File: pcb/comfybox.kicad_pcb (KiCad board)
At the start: 2 copper layers, 240 x 130 mm, 21 parts, among them K1 SW_CHOC, K2 SW_CHOC, K3 SW_CHOC, K4 SW_CHOC, P1 SW_CHOC, P2 SW_CHOC, P3 SW_CHOC, P4 SW_CHOC

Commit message: add front ground plane
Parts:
- moved G*** 1.00 mm to (217.5, 135.0)
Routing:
- added copper zone on F.Cu, net GND

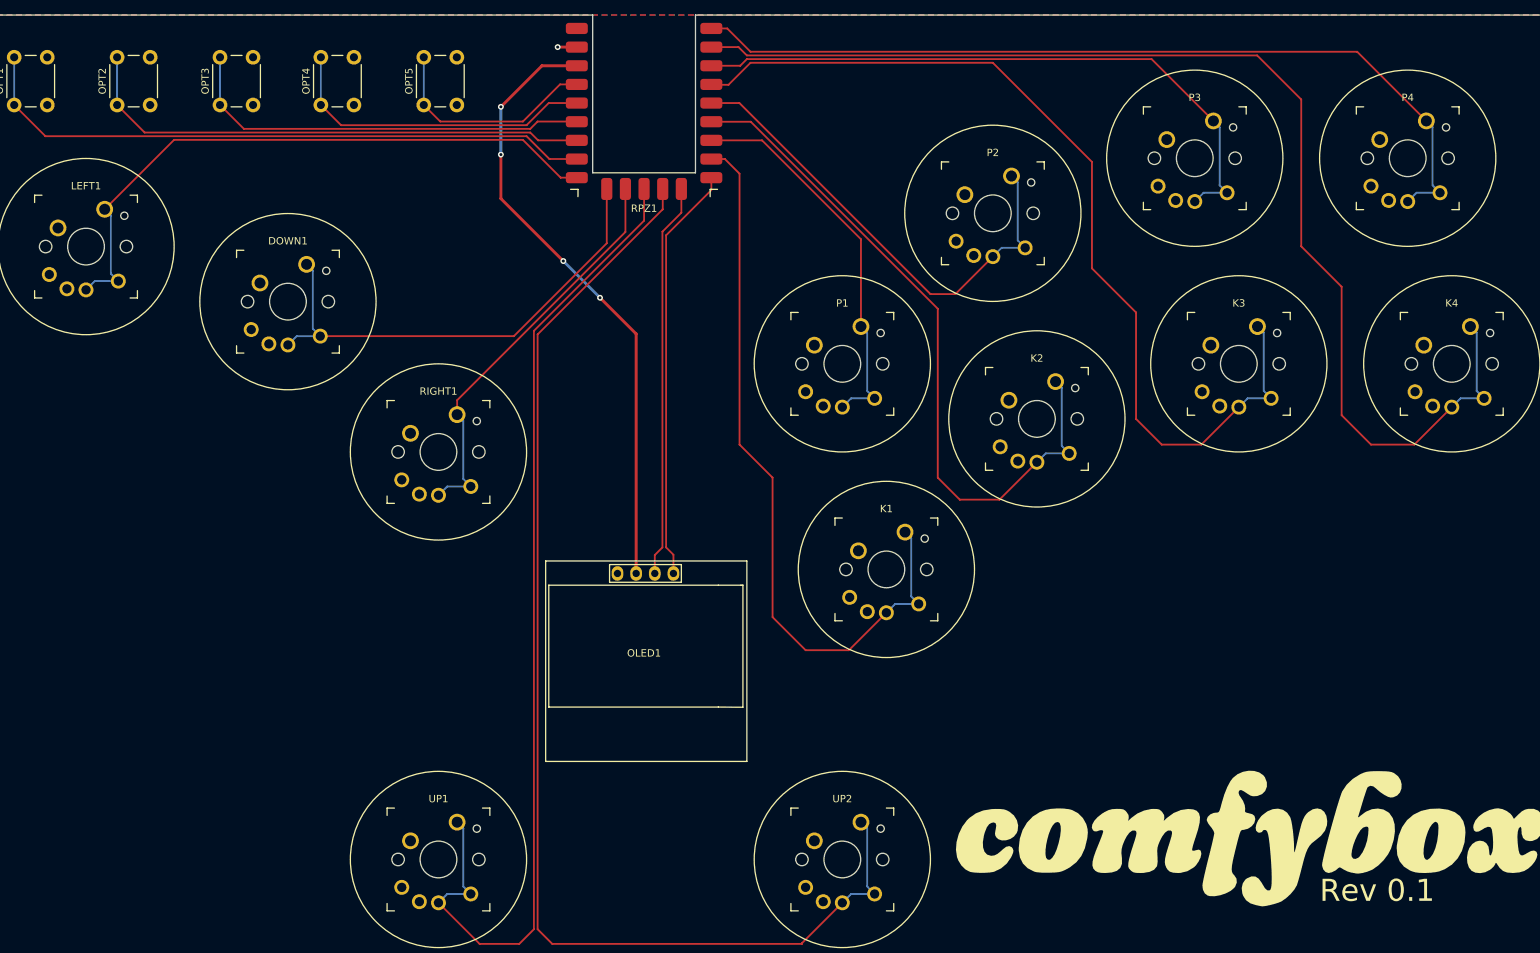
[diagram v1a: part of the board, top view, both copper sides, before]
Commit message: reversible rp2040
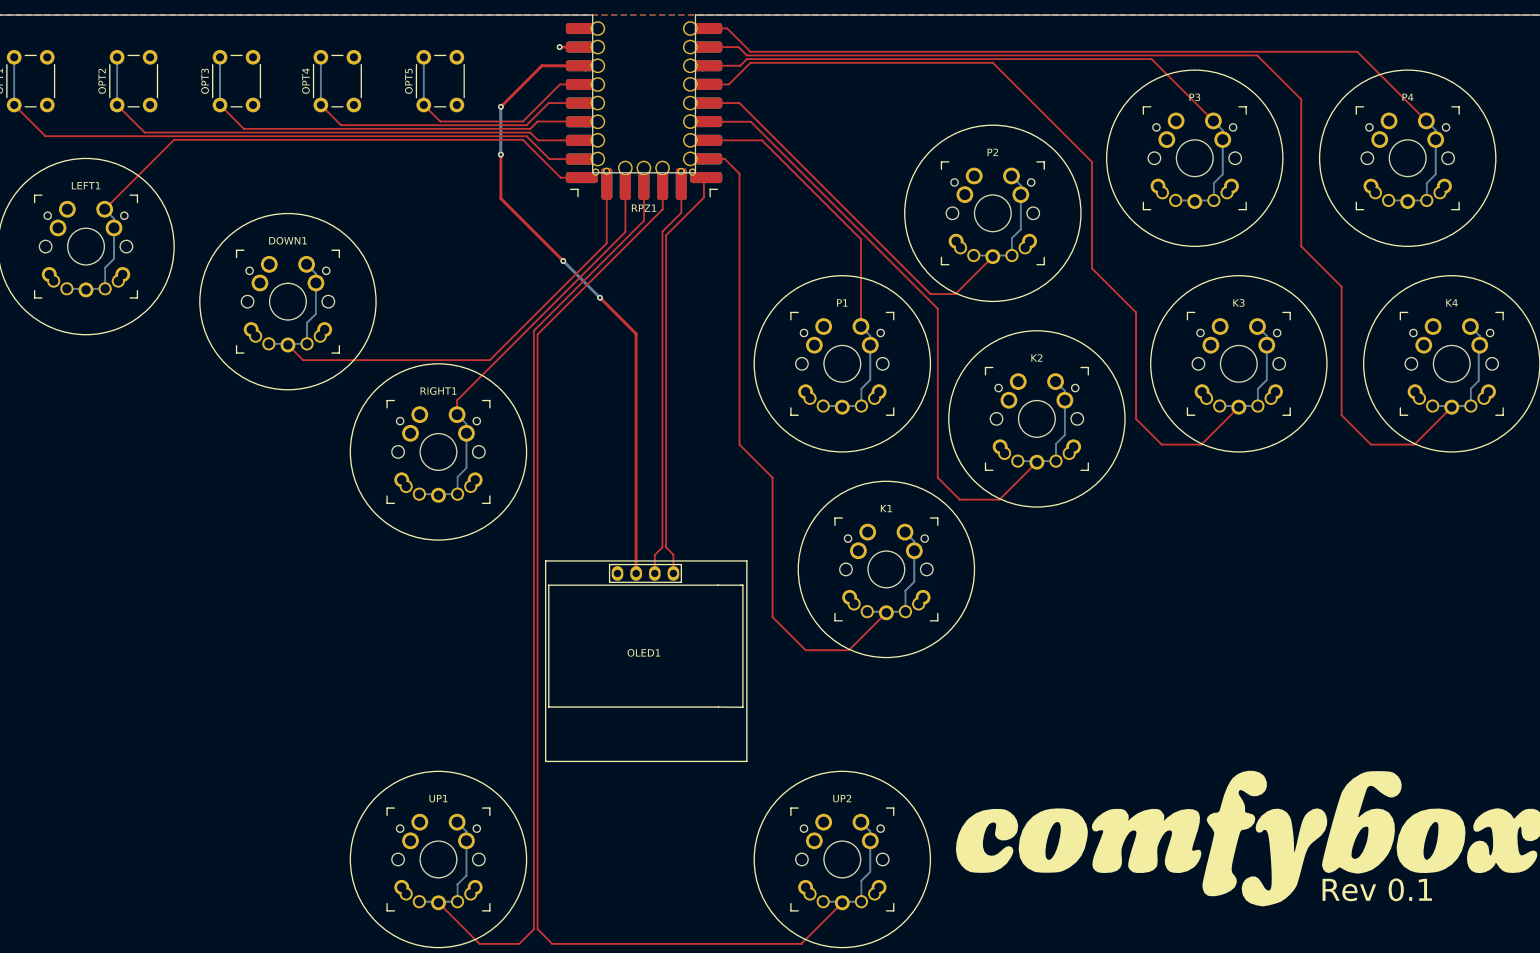
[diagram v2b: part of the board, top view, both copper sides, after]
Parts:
- DOWN1, K1, K2, K3, K4, LEFT1, P1, P2, P3, P4, RIGHT1, UP1, UP2: footprint Switch:Kailh_PG1350_Gateron_KS33_MX -> Switch:Kailh_PG1350_Gateron_KS33_MX_reversible
- RPZ1: footprint RP2040-Zero:RP2040-Zero -> RP2040-Zero:RP2040-Zero_reversible
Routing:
- net DOWN: track 67.1 -> 76.4 mm
- net P2: track 66.7 -> 69.4 mm
- net LEFT: track 85.8 -> 88.5 mm
- net P3: track 87.7 -> 90.4 mm
- net P1: track 53.3 -> 56.0 mm
- net P4: track 118.0 -> 120.8 mm
- net K2: track 96.7 -> 99.4 mm
- net K1: track 101.9 -> 104.6 mm
- net K4: track 162.8 -> 165.5 mm
- net UP R: track 168.0 -> 170.8 mm
- net RIGHT: track 55.7 -> 58.4 mm
- net UP L: track 138.6 -> 141.4 mm
- net K3: track 129.2 -> 131.9 mm
- net HOME: track 56.9 -> 58.9 mm
- net 3V3: track 83.8 -> 84.8 mm
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
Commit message: add back oled
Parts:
- added OLED2: SSD1306, OLED:SSD1306-128x64_OLED, B.Cu at (135.5, 113.2)
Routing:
- net OLED SDA: track 56.5 -> 72.3 mm
- net 3V3: track 84.8 -> 89.4 mm
- net OLED SCL: track 54.9 -> 59.4 mm
- net GND: track 2.35 -> 4.70 mm, vias 1 -> 0
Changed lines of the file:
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@@
       (net 2 "GND") (pinfunction "2") (pintype "passive"))
+  )
+  (footprint "OLED:SSD1306-128x64_OLED" (layer "B.Cu")
+    (at 135.5 113.15 180)
+    (property "Sheetfile" "comfybox.kicad_sch")
+    (property "Sheetname" "")
+    (attr through_hole)
+    (fp_text reference "OLED2" (at 0 -0.254) (layer "F.SilkS")
+        (effects (font (size 1 1) (thickness 0.15)))
+    )
+    (fp_text value "SSD1306" (at -7.747 7.62) (layer "F.Fab")
+        (effects (font (size 1 1) (thickness 0.15)))
+    )
+    (fp_line (start -13.4 -15) (end -13.4 12.3)
+      (stroke (width 0.12) (type solid)) (layer "B.SilkS"))
+    (fp_line (start -13.4 12.3) (end 14 12.3)
+      (stroke (width 0.12) (type solid)) (layer "B.SilkS"))
+    (fp_line (start -12.978 -7.595) (end -12.978 9.005)
+      (stroke (width 0.12) (type solid)) (layer "B.SilkS"))
+    (fp_line (start -12.978 9.005) (end 10.122 9.005)
+      (stroke (width 0.12) (type solid)) (layer "B.SilkS"))
+    (fp_line (start -4.699 11.811) (end -4.699 9.398)
+      (stroke (width 0.12) (type solid)) (layer "B.SilkS"))
+    (fp_line (start -4.699 11.811) (end 5.08 11.811)
+      (stroke (width 0.12) (type solid)) (layer "B.SilkS"))
+    (fp_line (start 5.08 9.398) (end -4.699 9.398)
+      (stroke (width 0.12) (type solid)) (layer "B.SilkS"))
+    (fp_line (start 5.08 11.811) (end 5.08 9.398)
+      (stroke (width 0.12) (type solid)) (layer "B.SilkS"))
+    (fp_line (start 10.122 -7.595) (end -12.978 -7.595)
+      (stroke (width 0.12) (type solid)) (layer "B.SilkS"))
+    (fp_line (start 10.122 -7.595) (end 13.462 -7.62)
+      (stroke (width 0.12) (type solid)) (layer "B.SilkS"))
+    (fp_line (start 10.122 9.005) (end 13.208 9.005)
+      (stroke (width 0.12) (type solid)) (layer "B.SilkS"))
+    (fp_line (start 13.462 -7.62) (end 13.462 9.017)
+      (stroke (width 0.12) (type solid)) (layer "B.SilkS"))
+    (fp_line (start 13.462 9.017) (end 13.208 9.005)
+      (stroke (width 0.12) (type solid)) (layer "B.SilkS"))
+    (fp_line (start 14 -15) (end -13.4 -15)
+      (stroke (width 0.12) (type solid)) (layer "B.SilkS"))
+    (fp_line (start 14 12.3) (end 14 -15)
+      (stroke (width 0.12) (type solid)) (layer "B.SilkS"))
+    (pad "1" thru_hole oval (at -3.62 10.6 90) (size 2 1.6) (drill 1) (layers "*.Cu" "*.Mask")
+      (net 2 "GND") (pinfunction "GND") (pintype "input"))
+    (pad "2" thru_hole oval (at -1.08 10.6 90) (size 2 1.6) (drill 1) (layers "*.Cu" "*.Mask")
+      (net 22 "3V3") (pinfunction "VCC") (pintype "input"))
+    (pad "3" thru_hole oval (at 1.46 10.6 90) (size 2 1.6) (drill 1) (layers "*.Cu" "*.Mask")
+      (net 21 "OLED SCL") (pinfunction "SCL") (pintype "input"))
+    (pad "4" thru_hole oval (at 4 10.6 90) (size 2 1.6) (drill 1) (layers "*.Cu" "*.Mask")
+      (net 20 "OLED SDA") (pinfunction "SDA") (pintype "input"))
   )
   (gr_circle (center 106.999466 82.5) (end 118.999466 82.5)
@@
   (segment (start 161.85 76.25) (end 162 76.4) (width 0.25) (layer "B.Cu") (net 1))
   (segment (start 165.81 66.69) (end 165.81 67.96) (width 0.25) (layer "B.Cu") (net 1))
+  (segment (start 125.845 27.365516) (end 125.85 27.360516) (width 0.4) (layer "F.Cu") (net 2))
   (segment (start 123.5 27.365516) (end 125.845 27.365516) (width 0.4) (layer "F.Cu") (net 2))
-  (segment (start 125.845 27.365516) (end 125.85 27.360516) (width 0.4) (layer "F.Cu") (net 2))
-  (via (at 123.5 27.365516) (size 0.8) (drill 0.4) (layers "F.Cu" "B.Cu") (net 2))
+  (segment (start 125.85 27.360516) (end 123.5 27.360516) (width 0.4) (layer "B.Cu") (net 2))
   (segment (start 177.399985 61) (end 174 61) (width 0.25) (layer "F.Cu") (net 3))
   (segment (start 147.985516 34.985516) (end 143.15 34.985516) (width 0.25) (layer "F.Cu") (net 3))
@@
   (segment (start 143.15 47.85) (end 143.15 45.145516) (width 0.25) (layer "F.Cu") (net 20))
   (segment (start 138 95.5) (end 138 53) (width 0.25) (layer "F.Cu") (net 20))
+  (segment (start 131 97) (end 129.5 98.5) (width 0.25) (layer "B.Cu") (net 20))
+  (segment (start 129.5 100.55) (end 131.5 102.55) (width 0.25) (layer "B.Cu") (net 20))
+  (segment (start 129.5 98.5) (end 129.5 100.55) (width 0.25) (layer "B.Cu") (net 20))
+  (segment (start 136.95 97) (end 131 97) (width 0.25) (layer "B.Cu") (net 20))
+  (segment (start 139 99.05) (end 136.95 97) (width 0.25) (layer "B.Cu") (net 20))
+  (segment (start 136.46 99.05) (end 136.46 100.13) (width 0.25) (layer "F.Cu") (net 21))
   (segment (start 140.08 49.92) (end 140.08 45.685516) (width 0.25) (layer "F.Cu") (net 21))
   (segment (start 137.5 52.5) (end 140.08 49.92) (width 0.25) (layer "F.Cu") (net 21))
   (segment (start 136.46 96.54) (end 137.5 95.5) (width 0.25) (layer "F.Cu") (net 21))
+  (segment (start 136.46 100.13) (end 134.04 102.55) (width 0.25) (layer "F.Cu") (net 21))
   (segment (start 137.5 95.5) (end 137.5 52.5) (width 0.25) (layer "F.Cu") (net 21))
   (segment (start 136.46 99.05) (end 136.46 96.54) (width 0.25) (layer "F.Cu") (net 21))
@@
   (via (at 124 56.5) (size 0.8) (drill 0.4) (layers "F.Cu" "B.Cu") (net 22))
   (via (at 115.5 35.5) (size 0.8) (drill 0.4) (layers "F.Cu" "B.Cu") (net 22))
+  (segment (start 133.92 99.89) (end 136.58 102.55) (width 0.4) (layer "B.Cu") (net 22))
+  (segment (start 133.92 99.05) (end 133.92 99.89) (width 0.4) (layer "B.Cu") (net 22))
   (segment (start 129 61.5) (end 124 56.5) (width 0.4) (layer "B.Cu") (net 22))
   (segment (start 115.5 42) (end 115.5 35.5) (width 0.4) (layer "B.Cu") (net 22))

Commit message: add back silk screen
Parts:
- added LOGO: LOGO, LOGO, B.Cu at (217.5, 135.0)
- renumbered G*** to LOGO

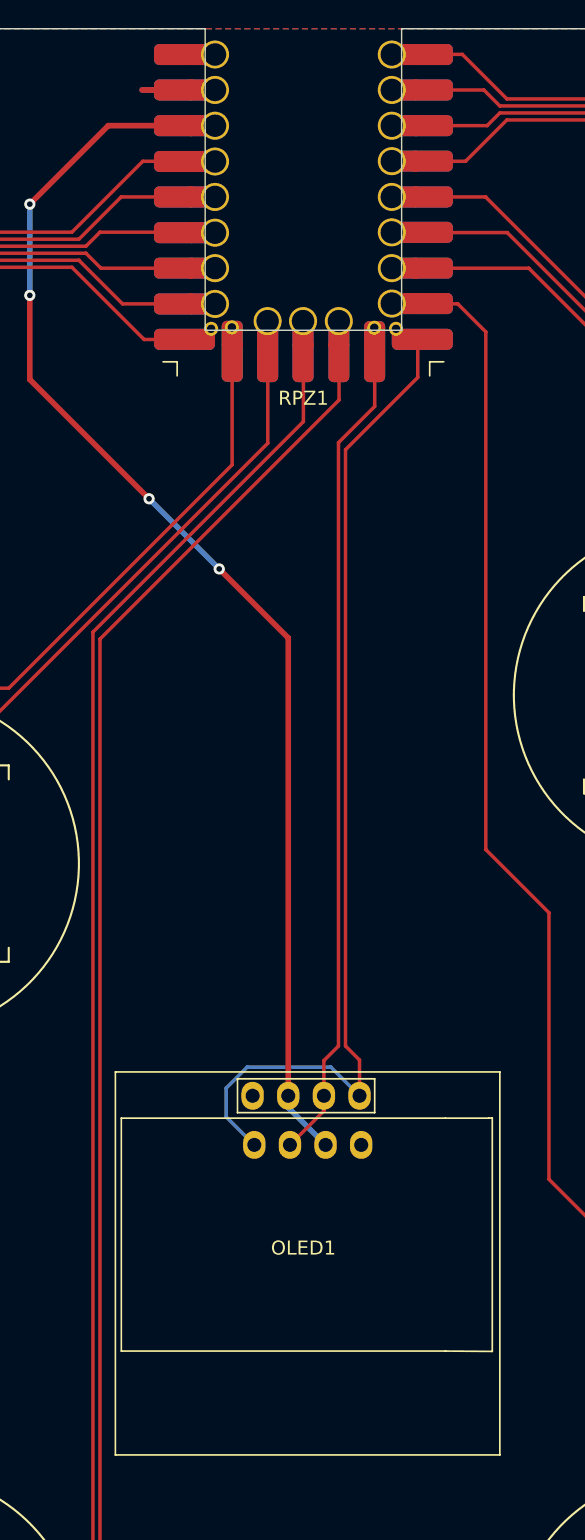
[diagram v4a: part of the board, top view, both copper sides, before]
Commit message: rework reversibility
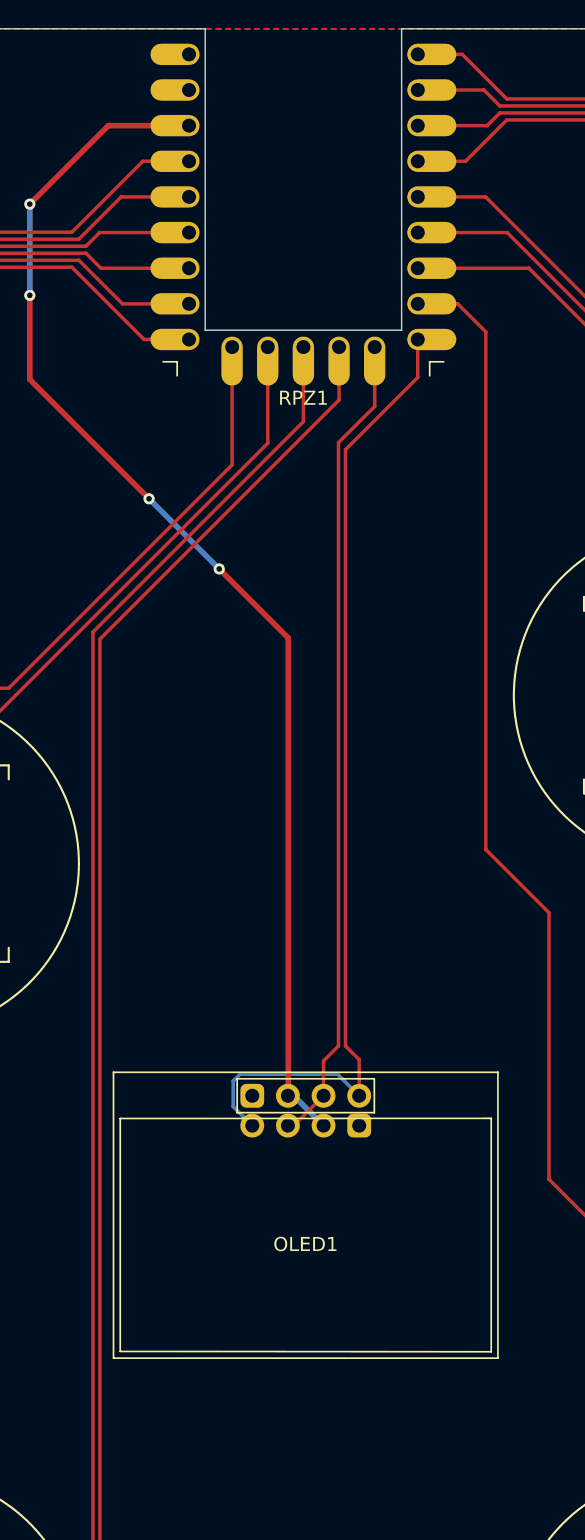
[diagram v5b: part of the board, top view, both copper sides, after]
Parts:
- removed OLED2: SSD1306, OLED:SSD1306-128x64_OLED
- OLED1: footprint OLED:SSD1306-128x64_OLED -> OLED:SSD1306-128x64_OLED_reversible
- moved OLED1 0.17 mm to (135.2, 109.7)
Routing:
- net GND: track 4.70 -> 0.01 mm
- net OLED SDA: track 72.3 -> 70.0 mm
- net 3V3: track 89.4 -> 88.3 mm
- net OLED SCL: track 59.4 -> 58.3 mm
- net HOME: track 58.9 -> 57.8 mm

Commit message: add mounting holes
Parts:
- added H1: MountingHole, MountingHole:MountingHole_4.3mm_M4, F.Cu at (28.0, 29.0)
- added H2: MountingHole, MountingHole:MountingHole_4.3mm_M4, F.Cu at (256.0, 29.0)
- added H3: MountingHole, MountingHole:MountingHole_4.3mm_M4, F.Cu at (28.0, 147.0)
- added H4: MountingHole, MountingHole:MountingHole_4.3mm_M4, F.Cu at (142.0, 147.0)
- added H5: MountingHole, MountingHole:MountingHole_4.3mm_M4, F.Cu at (256.0, 147.0)
- added H6: MountingHole, MountingHole:MountingHole_4.3mm_M4, F.Cu at (163.5, 37.0)
- moved LOGO 2.50 mm to (217.5, 137.5) (x2)
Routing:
- net UP R: track 170.8 -> 185.0 mm
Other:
- board text added: "GND"

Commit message: update footprints
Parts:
- DOWN1, K1, K2, K3, K4, LEFT1, P1, P2, P3, P4, RIGHT1, UP1, UP2: footprint Switch:Kailh_PG1350_Gateron_KS33_MX_reversible -> Switch:Kailh_CPG1353_Gateron_KS33_MX_reversible
- H1, H2, H3, H4, H5, H6: footprint MountingHole:MountingHole_4.3mm_M4 -> MountingHole:MountingHole_4mm
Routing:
- net GND: track 0.01 -> 39.9 mm

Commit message: add repo link
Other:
- board text added: "github.com/okkdev/comfybox"
